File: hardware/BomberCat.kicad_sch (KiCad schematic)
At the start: 86 parts, among them J1 Battery, J3 MAGSPOOF, P1 USB_C_Plug_USB2.0, Q1 DMG3415U-7, SW1 RESET, SW2 GPIO, SW3 ON, SW4 SOURCE MAG, U1 PN7150B0HN_C11002E-PN7150B0HN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, U2 RP2040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

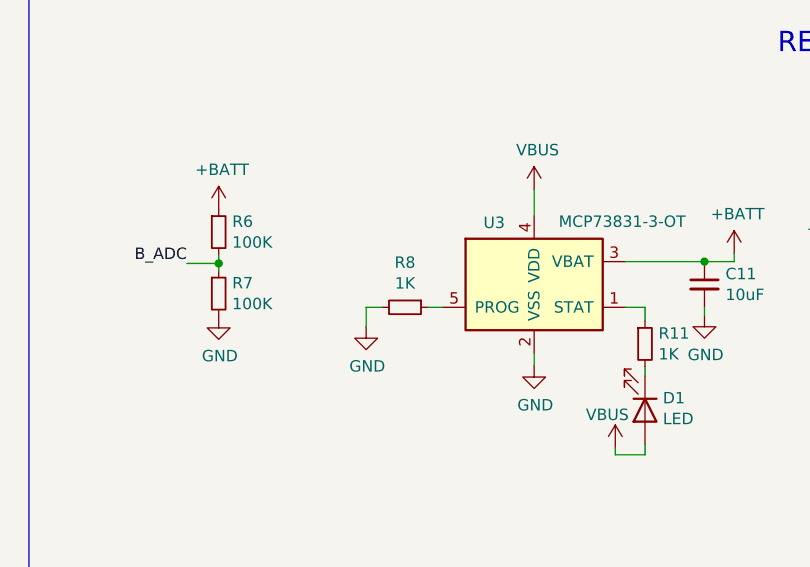
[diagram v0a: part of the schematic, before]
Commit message: change resistor charger
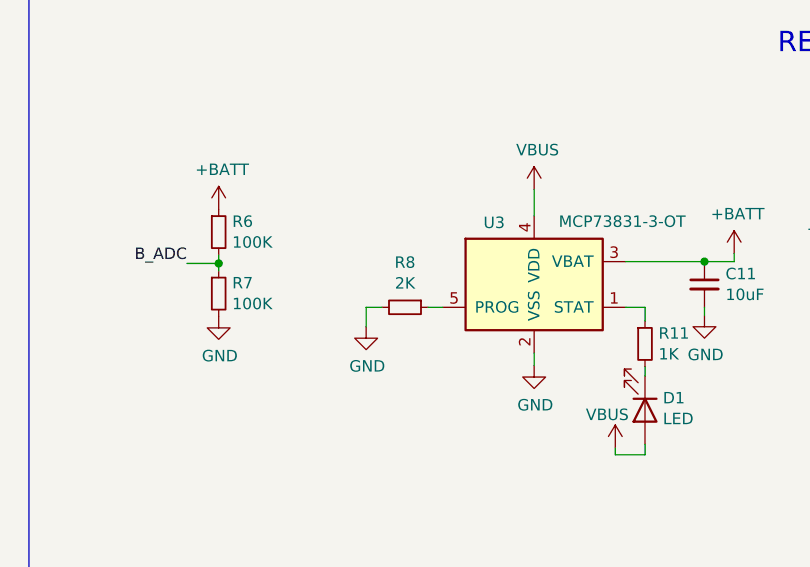
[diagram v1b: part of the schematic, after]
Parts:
- R8: value 1K -> 2K; LCSC# C112433 -> C25590
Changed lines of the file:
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@@
     (in_bom yes) (on_board yes)
     (property "Reference" "R8" (id 0) (at 108.839 248.5136 90))
-    (property "Value" "1K" (id 1) (at 108.839 250.825 90))
+    (property "Value" "2K" (id 1) (at 108.839 250.825 90))
     (property "Footprint" "Resistor_SMD:R_0603_1608Metric" (id 2) (at 108.839 253.492 0)
       (effects (font (size 1.27 1.27)) hide)
     )
-    (property "Datasheet" "https://datasheet.lcsc.com/lcsc/1811151132_Walsin-Tech-Corp-WR06X1001FTL_C112433.pdf" (id 3) (at 108.839 253.492 0)
+    (property "Datasheet" "https://datasheet.lcsc.com/lcsc/2206010100_UNI-ROYAL-Uniroyal-Elec-0603WAJ0202T5E_C25590.pdf" (id 3) (at 108.839 253.492 0)
       (effects (font (size 1.27 1.27)) hide)
     )
@@
       (effects (font (size 1.27 1.27)) hide)
     )
-    (property "LCSC#" "C112433" (id 5) (at 108.839 253.492 0)
+    (property "LCSC#" "C25590" (id 5) (at 108.839 253.492 0)
       (effects (font (size 1.27 1.27)) hide)
     )
@@
     )
     (path "/a94ab534-d026-4356-be23-1a7c1fc1e5f5"
-      (reference "R8") (unit 1) (value "1K") (footprint "Resistor_SMD:R_0603_1608Metric")
+      (reference "R8") (unit 1) (value "2K") (footprint "Resistor_SMD:R_0603_1608Metric")
     )
     (path "/07bf17f3-6a63-4322-b714-110b290ef65b"

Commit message: update fuse footprint
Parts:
- F1: footprint Fuse:Fuse_0603_1608Metric_Pad1.05x0.95mm_HandSolder -> Fuse:Fuse_0805_2012Metric
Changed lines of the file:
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@@
     (property "Reference" "F1" (id 0) (at 51.054 228.727 0))
     (property "Value" "0.5A" (id 1) (at 51.054 231.0384 0))
-    (property "Footprint" "Fuse:Fuse_0603_1608Metric_Pad1.05x0.95mm_HandSolder" (id 2) (at 51.054 233.426 0)
+    (property "Footprint" "Fuse:Fuse_0805_2012Metric" (id 2) (at 51.054 233.426 0)
       (effects (font (size 1.27 1.27)) hide)
     )
@@
     )
     (path "/7941b52a-c063-4364-bd55-27eea150373c"
-      (reference "F1") (unit 1) (value "0.5A") (footprint "Fuse:Fuse_0603_1608Metric_Pad1.05x0.95mm_HandSolder")
+      (reference "F1") (unit 1) (value "0.5A") (footprint "Fuse:Fuse_0805_2012Metric")
     )
     (path "/3e52c366-4ba8-4bd3-a04e-524d188005fb"

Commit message: Changed resistor R8 to 5.1K and updated BOM
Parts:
- C1, C2: value 27pF -> (none); footprint Capacitor_SMD:C_0603_1608Metric -> (none)
- C10, C14, C5, C6, C8: value 1uF -> (none); footprint Capacitor_SMD:C_0603_1608Metric -> (none)
- C11, C22, C29: value 10uF -> (none); footprint Capacitor_SMD:C_0603_1608Metric -> (none)
- C12, C13, C15, C16, C17, C18, C19, C20, C21, C32, C33, C7, C9: value 100nF -> (none); footprint Capacitor_SMD:C_0603_1608Metric -> (none)
- C23, C24: value 1nF/16V -> (none); footprint Capacitor_SMD:C_0603_1608Metric -> (none)
- C25, C26: value 680pF -> (none); footprint Capacitor_SMD:C_0603_1608Metric -> (none)
- C27, C28: value 100pF/50V -> (none); footprint Capacitor_SMD:C_0603_1608Metric -> (none)
- C3, C4: value 10pF -> (none); footprint Capacitor_SMD:C_0603_1608Metric -> (none)
- C30, C31: value 120pF -> (none); footprint Capacitor_SMD:C_0603_1608Metric -> (none)
- C34: value 10uf -> (none); footprint Capacitor_SMD:C_0603_1608Metric -> (none)
- D1, D2, D3: value LED -> (none); footprint LED_SMD:LED_0805_2012Metric_Pad1.15x1.40mm_HandSolder -> (none)
- D4: value MBR120 -> (none); footprint Diode_SMD:D_SOD-123F -> (none)
- F1: value 0.5A -> (none); footprint Fuse:Fuse_0805_2012Metric -> (none)
- H1, H2, H3, H4: value MountingHole -> (none); footprint MountingHole:MountingHole_2.2mm_M2 -> (none)
- J1: value Battery -> (none); footprint Connector_PinHeader_2.54mm:PinHeader_1x02_P2.54mm_Vertical -> (none)
- J3: value MAGSPOOF -> (none); footprint Connector_PinHeader_2.54mm:PinHeader_1x02_P2.54mm_Vertical -> (none)
- JP1: value BOOT -> (none); footprint Jumper:SolderJumper-2_P1.3mm_Open_TrianglePad1.0x1.5mm -> (none)
- L1, L2: value 160nH -> (none); footprint Inductor_SMD:L_0603_1608Metric_Pad1.05x0.95mm_HandSolder -> (none)
- L3: value L -> (none); footprint Connectors:MOLEX_1661 -> (none)
- P1: value USB_C_Plug_USB2.0 -> (none); footprint Connectors:C393939 -> (none)
- Q1: value DMG3415U-7 -> (none); footprint Package_TO_SOT_SMD:SOT-23 -> (none)
- R1, R17, R2, R20: value 10K -> (none); footprint Resistor_SMD:R_0603_1608Metric -> (none)
- R10, R9: value 27 -> (none); footprint Resistor_SMD:R_0603_1608Metric -> (none)
- R11, R12, R13, R3: value 1K -> (none); footprint Resistor_SMD:R_0603_1608Metric -> (none)
- R14, R21, R22, R6, R7: value 100K -> (none); footprint Resistor_SMD:R_0603_1608Metric -> (none)
- R15, R16: value 2k2 -> (none); footprint Resistor_SMD:R_0603_1608Metric -> (none)
- R18, R19: value 3.24R -> (none); footprint Resistor_SMD:R_0603_1608Metric -> (none)
- R4, R5: value 5k1 -> (none); footprint Resistor_SMD:R_0603_1608Metric -> (none)
- R8: value 2K -> (none); footprint Resistor_SMD:R_0603_1608Metric -> (none); LCSC# C25590 -> C73801; manf# WR06X1001FTL -> RS-03K512KT
- SW1: value RESET -> (none); footprint Button_Switch_SMD:SW_SPST_TL3342 -> (none)
- SW2: value GPIO -> (none); footprint Button_Switch_SMD:SW_SPST_TL3342 -> (none)
- SW3: value ON -> (none); footprint BomberCat:JS102011SAQN -> (none)
- SW4: value SOURCE MAG -> (none); footprint BomberCat:JS202011CQN -> (none)
- U1: value PN7150B0HN_C11002E-PN7150B0HN_C11002E -> (none); footprint Package_DFN_QFN:QFN-40-1EP_6x6mm_P0.5mm_EP4.6x4.6mm -> (none)
- U2: value RP2040 -> (none); footprint BomberCat:RP2040-QFN-56 -> (none)
- U3: value MCP73831-3-OT -> (none); footprint Package_TO_SOT_SMD:SOT-23-5 -> (none)
- U4: value AP2112K-3.3 -> (none); footprint Package_TO_SOT_SMD:SOT-23-5 -> (none)
- U5: value ESP32-WROOM-32D -> (none); footprint RF_Module:ESP32-WROOM-32 -> (none)
- U6: value W25Q16JV -> (none); footprint BomberCat:W25Q16JVUUIQ -> (none)
- U7: value TC4424 -> (none); footprint Package_SO:SOIC-8_3.9x4.9mm_P1.27mm -> (none)
- Y1: value 27.12Mhz -> (none); footprint Crystal:Crystal_SMD_2016-4Pin_2.0x1.6mm -> (none)
- Y2: value 12Mhz -> (none); footprint Crystal:Crystal_SMD_5032-2Pin_5.0x3.2mm -> (none)

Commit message: Update version schematic
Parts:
- C1, C2: value (none) -> 27pF; footprint (none) -> Capacitor_SMD:C_0603_1608Metric
- C10, C14, C5, C6, C8: value (none) -> 1uF; footprint (none) -> Capacitor_SMD:C_0603_1608Metric
- C11, C22, C29: value (none) -> 10uF; footprint (none) -> Capacitor_SMD:C_0603_1608Metric
- C12, C13, C15, C16, C17, C18, C19, C20, C21, C32, C33, C7, C9: value (none) -> 100nF; footprint (none) -> Capacitor_SMD:C_0603_1608Metric
- C23, C24: value (none) -> 1nF/16V; footprint (none) -> Capacitor_SMD:C_0603_1608Metric
- C25, C26: value (none) -> 680pF; footprint (none) -> Capacitor_SMD:C_0603_1608Metric
- C27, C28: value (none) -> 100pF/50V; footprint (none) -> Capacitor_SMD:C_0603_1608Metric
- C3, C4: value (none) -> 10pF; footprint (none) -> Capacitor_SMD:C_0603_1608Metric
- C30, C31: value (none) -> 120pF; footprint (none) -> Capacitor_SMD:C_0603_1608Metric
- C34: value (none) -> 10uf; footprint (none) -> Capacitor_SMD:C_0603_1608Metric
- D1, D2, D3: value (none) -> LED; footprint (none) -> LED_SMD:LED_0805_2012Metric_Pad1.15x1.40mm_HandSolder
- D4: value (none) -> MBR120; footprint (none) -> Diode_SMD:D_SOD-123F
- F1: value (none) -> 0.5A; footprint (none) -> Fuse:Fuse_0805_2012Metric
- H1, H2, H3, H4: value (none) -> MountingHole; footprint (none) -> MountingHole:MountingHole_2.2mm_M2
- J1: value (none) -> Battery; footprint (none) -> Connector_PinHeader_2.54mm:PinHeader_1x02_P2.54mm_Vertical
- J3: value (none) -> MAGSPOOF; footprint (none) -> Connector_PinHeader_2.54mm:PinHeader_1x02_P2.54mm_Vertical
- JP1: value (none) -> BOOT; footprint (none) -> Jumper:SolderJumper-2_P1.3mm_Open_TrianglePad1.0x1.5mm
- L1, L2: value (none) -> 160nH; footprint (none) -> Inductor_SMD:L_0603_1608Metric_Pad1.05x0.95mm_HandSolder
- L3: value (none) -> L; footprint (none) -> Connectors:MOLEX_1661
- P1: value (none) -> USB_C_Plug_USB2.0; footprint (none) -> Connectors:C393939
- Q1: value (none) -> DMG3415U-7; footprint (none) -> Package_TO_SOT_SMD:SOT-23
- R1, R17, R2, R20: value (none) -> 10K; footprint (none) -> Resistor_SMD:R_0603_1608Metric
- R10, R9: value (none) -> 27; footprint (none) -> Resistor_SMD:R_0603_1608Metric
- R11, R12, R13, R3: value (none) -> 1K; footprint (none) -> Resistor_SMD:R_0603_1608Metric
- R14, R21, R22, R6, R7: value (none) -> 100K; footprint (none) -> Resistor_SMD:R_0603_1608Metric
- R15, R16: value (none) -> 2k2; footprint (none) -> Resistor_SMD:R_0603_1608Metric
- R18, R19: value (none) -> 3.24R; footprint (none) -> Resistor_SMD:R_0603_1608Metric
- R4, R5: value (none) -> 5k1; footprint (none) -> Resistor_SMD:R_0603_1608Metric
- R8: value (none) -> 5.1K; footprint (none) -> Resistor_SMD:R_0603_1608Metric
- SW1: value (none) -> RESET; footprint (none) -> Button_Switch_SMD:SW_SPST_TL3342
- SW2: value (none) -> GPIO; footprint (none) -> Button_Switch_SMD:SW_SPST_TL3342
- SW3: value (none) -> ON; footprint (none) -> BomberCat:JS102011SAQN
- SW4: value (none) -> SOURCE MAG; footprint (none) -> BomberCat:JS202011CQN
- U1: value (none) -> PN7150B0HN_C11002E-PN7150B0HN_C11002E; footprint (none) -> Package_DFN_QFN:QFN-40-1EP_6x6mm_P0.5mm_EP4.6x4.6mm
- U2: value (none) -> RP2040; footprint (none) -> BomberCat:RP2040-QFN-56
- U3: value (none) -> MCP73831-3-OT; footprint (none) -> Package_TO_SOT_SMD:SOT-23-5
- U4: value (none) -> AP2112K-3.3; footprint (none) -> Package_TO_SOT_SMD:SOT-23-5
- U5: value (none) -> ESP32-WROOM-32D; footprint (none) -> RF_Module:ESP32-WROOM-32
- U6: value (none) -> W25Q16JV; footprint (none) -> BomberCat:W25Q16JVUUIQ
- U7: value (none) -> TC4424; footprint (none) -> Package_SO:SOIC-8_3.9x4.9mm_P1.27mm
- Y1: value (none) -> 27.12Mhz; footprint (none) -> Crystal:Crystal_SMD_2016-4Pin_2.0x1.6mm
- Y2: value (none) -> 12Mhz; footprint (none) -> Crystal:Crystal_SMD_5032-2Pin_5.0x3.2mm

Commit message: add BOM connector antenna
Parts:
- L3: manf# - -> CONUFL001-SMD; provedor - -> Mouser
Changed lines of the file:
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@@
       (effects (font (size 1.27 1.27)) hide)
     )
-    (property "manf#" "-" (id 5) (at 256.032 50.673 0)
+    (property "manf#" "CONUFL001-SMD" (id 5) (at 256.032 50.673 0)
       (effects (font (size 1.27 1.27)) hide)
     )
-    (property "provedor" "-" (id 6) (at 256.032 50.673 0)
+    (property "provedor" "Mouser" (id 6) (at 256.032 50.673 0)
       (effects (font (size 1.27 1.27)) hide)
     )
